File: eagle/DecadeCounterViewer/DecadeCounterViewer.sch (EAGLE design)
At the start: 16 parts, among them IC1 CD4017

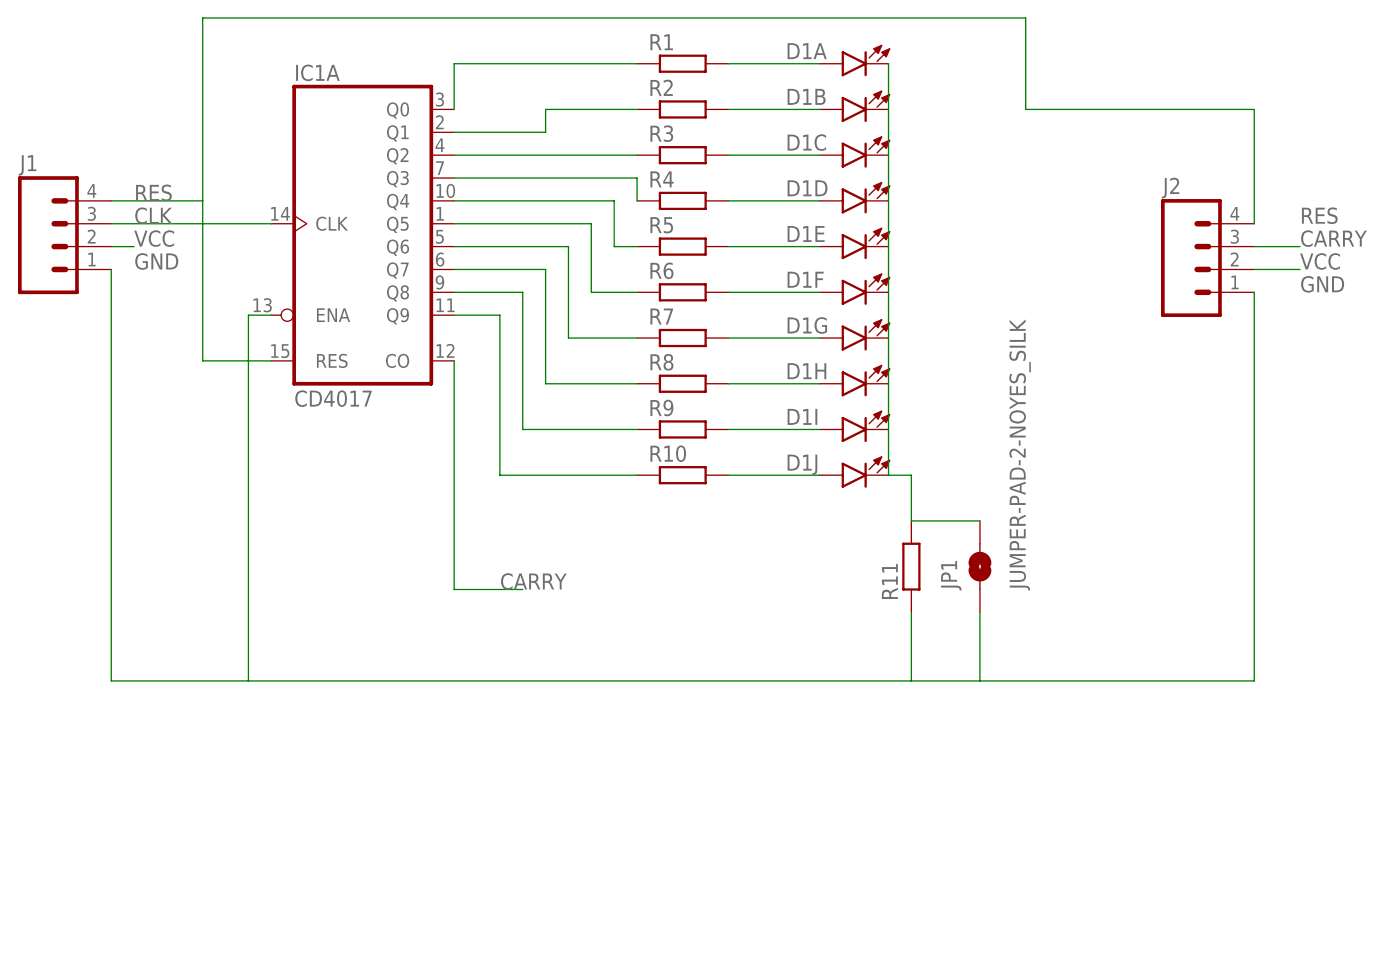
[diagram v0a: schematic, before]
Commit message: Decade counter continued
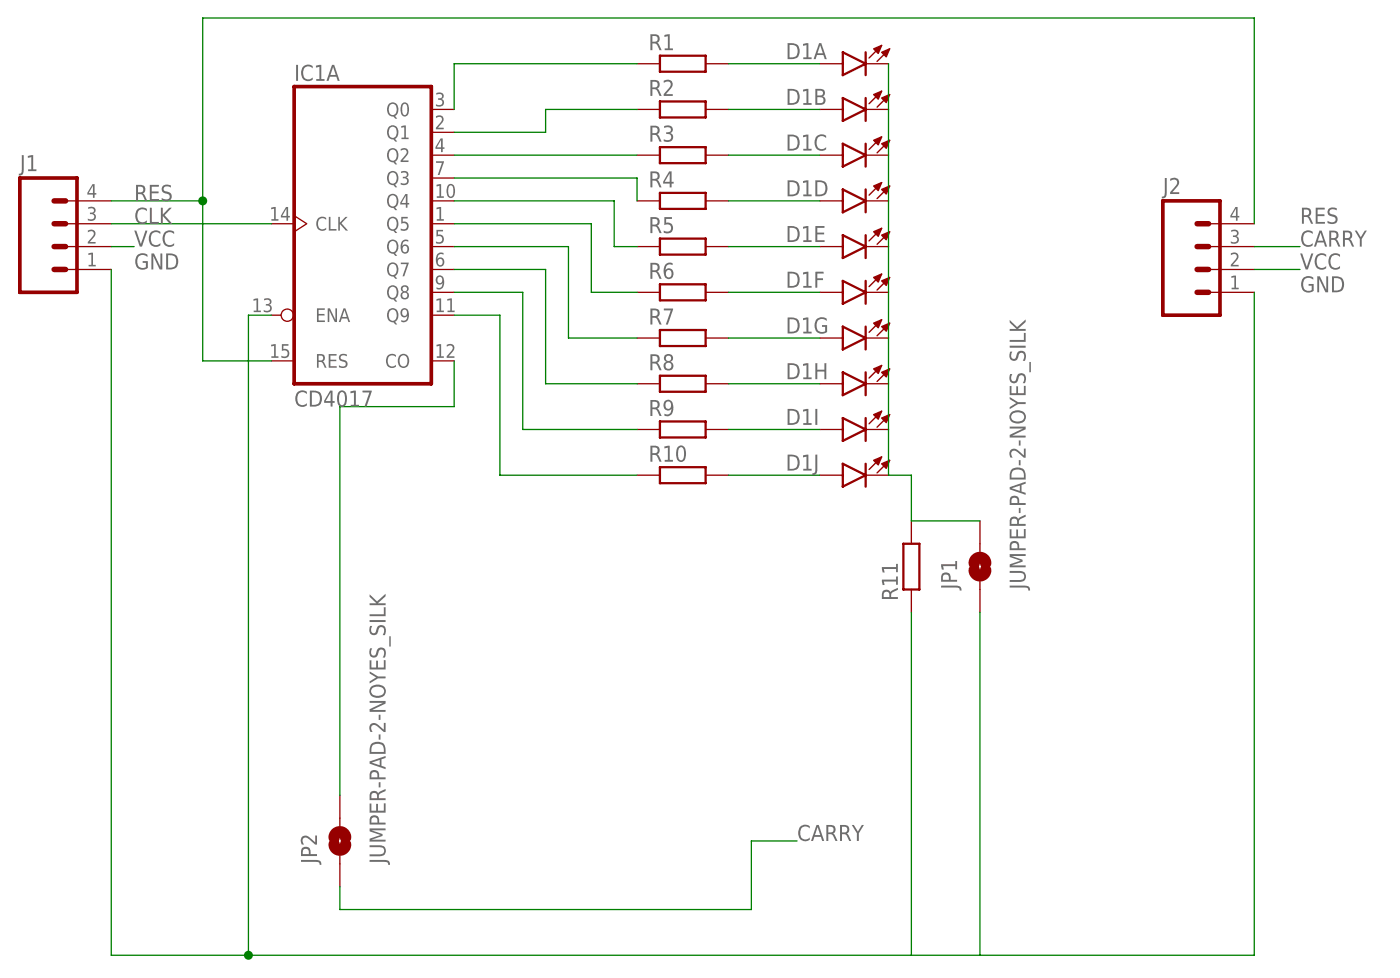
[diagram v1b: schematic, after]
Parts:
- added JP2: JUMPER-PAD-2-NOYES_SILK, SparkFun-Passives:JUMPER-PAD-2-NOYES_SILK
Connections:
- new net N$1: IC1A.CO, JP2.2
- net CARRY: now also JP2.1; no longer IC1A.CO
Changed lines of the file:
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@@
 <part name="J1" library="SparkFun-Connectors" deviceset="M04" device="LOCK"/>
 <part name="J2" library="SparkFun-Connectors" deviceset="M04" device="LOCK"/>
+<part name="JP2" library="SparkFun-Passives" deviceset="JUMPER-PAD-2-NO" device="YES_SILK"/>
 </parts>
 <sheets>
@@
 <instance part="J1" gate="G$1" x="-7.62" y="83.82"/>
 <instance part="J2" gate="G$1" x="119.38" y="81.28"/>
+<instance part="JP2" gate="G$1" x="22.86" y="17.78" rot="R90"/>
 </instances>
 <busses>
@@
 <segment>
 <pinref part="J1" gate="G$1" pin="1"/>
-<wire x1="-2.54" y1="81.28" x2="-2.54" y2="35.56" width="0.1524" layer="91"/>
+<wire x1="-2.54" y1="81.28" x2="-2.54" y2="5.08" width="0.1524" layer="91"/>
 <pinref part="R11" gate="G$1" pin="1"/>
-<wire x1="-2.54" y1="35.56" x2="12.7" y2="35.56" width="0.1524" layer="91"/>
-<wire x1="12.7" y1="35.56" x2="86.36" y2="35.56" width="0.1524" layer="91"/>
-<wire x1="86.36" y1="35.56" x2="86.36" y2="43.18" width="0.1524" layer="91"/>
+<wire x1="-2.54" y1="5.08" x2="12.7" y2="5.08" width="0.1524" layer="91"/>
+<wire x1="12.7" y1="5.08" x2="86.36" y2="5.08" width="0.1524" layer="91"/>
+<wire x1="86.36" y1="5.08" x2="86.36" y2="43.18" width="0.1524" layer="91"/>
 <pinref part="JP1" gate="G$1" pin="1"/>
-<wire x1="86.36" y1="35.56" x2="93.98" y2="35.56" width="0.1524" layer="91"/>
-<wire x1="93.98" y1="35.56" x2="93.98" y2="43.18" width="0.1524" layer="91"/>
+<wire x1="86.36" y1="5.08" x2="93.98" y2="5.08" width="0.1524" layer="91"/>
+<wire x1="93.98" y1="5.08" x2="93.98" y2="43.18" width="0.1524" layer="91"/>
 <label x="0" y="81.28" size="1.778" layer="95"/>
 <pinref part="IC1" gate="A" pin="ENA"/>
 <wire x1="15.24" y1="76.2" x2="12.7" y2="76.2" width="0.1524" layer="91"/>
-<wire x1="12.7" y1="76.2" x2="12.7" y2="35.56" width="0.1524" layer="91"/>
+<wire x1="12.7" y1="76.2" x2="12.7" y2="5.08" width="0.1524" layer="91"/>
 <pinref part="J2" gate="G$1" pin="1"/>
-<wire x1="93.98" y1="35.56" x2="124.46" y2="35.56" width="0.1524" layer="91"/>
-<wire x1="124.46" y1="35.56" x2="124.46" y2="78.74" width="0.1524" layer="91"/>
+<wire x1="93.98" y1="5.08" x2="124.46" y2="5.08" width="0.1524" layer="91"/>
+<wire x1="124.46" y1="5.08" x2="124.46" y2="78.74" width="0.1524" layer="91"/>
 <label x="129.54" y="78.74" size="1.778" layer="95"/>
+<junction x="12.7" y="5.08"/>
 </segment>
 </net>
@@
 <net name="CARRY" class="0">
 <segment>
-<pinref part="IC1" gate="A" pin="CO"/>
-<wire x1="35.56" y1="71.12" x2="35.56" y2="45.72" width="0.1524" layer="91"/>
-<wire x1="35.56" y1="45.72" x2="43.18" y2="45.72" width="0.1524" layer="91"/>
-<label x="40.64" y="45.72" size="1.778" layer="95"/>
+<wire x1="68.58" y1="17.78" x2="73.66" y2="17.78" width="0.1524" layer="91"/>
+<label x="73.66" y="17.78" size="1.778" layer="95"/>
+<pinref part="JP2" gate="G$1" pin="1"/>
+<wire x1="22.86" y1="12.7" x2="22.86" y2="10.16" width="0.1524" layer="91"/>
+<wire x1="22.86" y1="10.16" x2="68.58" y2="10.16" width="0.1524" layer="91"/>
+<wire x1="68.58" y1="10.16" x2="68.58" y2="17.78" width="0.1524" layer="91"/>
 </segment>
 <segment>
@@
 <label x="0" y="88.9" size="1.778" layer="95"/>
 <wire x1="7.62" y1="88.9" x2="7.62" y2="109.22" width="0.1524" layer="91"/>
-<wire x1="7.62" y1="109.22" x2="99.06" y2="109.22" width="0.1524" layer="91"/>
-<wire x1="99.06" y1="109.22" x2="99.06" y2="99.06" width="0.1524" layer="91"/>
+<wire x1="7.62" y1="109.22" x2="124.46" y2="109.22" width="0.1524" layer="91"/>
 <pinref part="J2" gate="G$1" pin="4"/>
-<wire x1="99.06" y1="99.06" x2="124.46" y2="99.06" width="0.1524" layer="91"/>
-<wire x1="124.46" y1="99.06" x2="124.46" y2="86.36" width="0.1524" layer="91"/>
+<wire x1="124.46" y1="109.22" x2="124.46" y2="86.36" width="0.1524" layer="91"/>
 <label x="129.54" y="86.36" size="1.778" layer="95"/>
-</segment>
-</net>
+<junction x="7.62" y="88.9"/>
+</segment>
+</net>
+<net name="N$1" class="0">
+<segment>
+<pinref part="IC1" gate="A" pin="CO"/>
+<wire x1="35.56" y1="71.12" x2="35.56" y2="66.04" width="0.1524" layer="91"/>
+<wire x1="35.56" y1="66.04" x2="22.86" y2="66.04" width="0.1524" layer="91"/>
+<pinref part="JP2" gate="G$1" pin="2"/>
+<wire x1="22.86" y1="66.04" x2="22.86" y2="22.86" width="0.1524" layer="91"/>
+</segment>
+</net>

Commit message: Added the decade counter board. Todo review and then send to production.
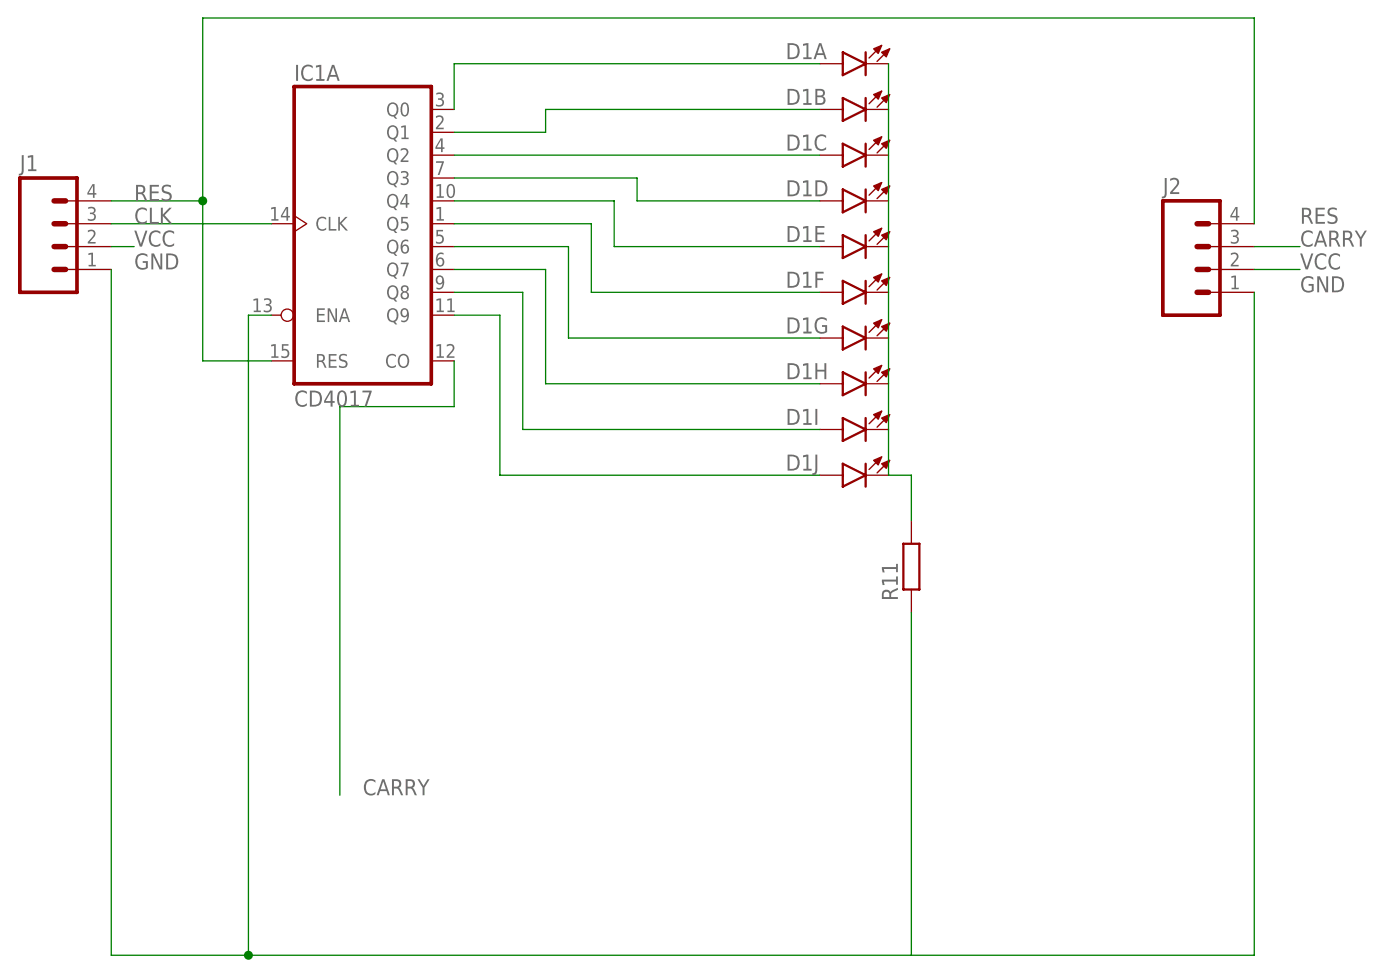
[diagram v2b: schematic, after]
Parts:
- removed JP1, JP2: JUMPER-PAD-2-NOYES_SILK, SparkFun-Passives:JUMPER-PAD-2-NOYES_SILK
- removed R1, R10, R2, R3, R4, R5, R6, R7, R8, R9: (no value), resistor:R-EU_R1206
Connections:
- removed net N$1: IC1A.CO, JP2.2
- removed net N$10: D1H.A, R8.2
- removed net N$11: D1I.A, R9.2
- removed net N$12: D1J.A, R10.2
- removed net N$3: D1A.A, R1.2
- removed net N$4: D1B.A, R2.2
- removed net N$5: D1C.A, R3.2
- removed net N$6: D1D.A, R4.2
- removed net N$7: D1E.A, R5.2
- removed net N$8: D1F.A, R6.2
- removed net N$9: D1G.A, R7.2
- net CARRY: now also IC1A.CO; no longer JP2.1
- net GND: no longer JP1.1
- net N$13: now also D1A.A; no longer R1.1
- net N$14: now also D1B.A; no longer R2.1
- net N$15: now also D1C.A; no longer R3.1
- net N$16: now also D1D.A; no longer R4.1
- net N$17: now also D1E.A; no longer R5.1
- net N$18: now also D1F.A; no longer R6.1
- net N$19: now also D1G.A; no longer R7.1
- net N$2: no longer JP1.2
- net N$20: now also D1H.A; no longer R8.1
- net N$21: now also D1I.A; no longer R9.1
- net N$22: now also D1J.A; no longer R10.1

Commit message: Added labels, reviewed. Ok for prod.
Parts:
- added R1: (no value), resistor:R-EU_0204/7
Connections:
- net GND: now also R1.1
- net N$2: now also R1.2
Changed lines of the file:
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@@
 <part name="J1" library="SparkFun-Connectors" deviceset="M04" device="LOCK"/>
 <part name="J2" library="SparkFun-Connectors" deviceset="M04" device="LOCK"/>
+<part name="R1" library="resistor" deviceset="R-EU_" device="0204/7"/>
 </parts>
 <sheets>
@@
 <instance part="J1" gate="G$1" x="-7.62" y="83.82"/>
 <instance part="J2" gate="G$1" x="119.38" y="81.28"/>
+<instance part="R1" gate="G$1" x="93.98" y="48.26" rot="R90"/>
 </instances>
 <busses>
@@
 <label x="129.54" y="78.74" size="1.778" layer="95"/>
 <junction x="12.7" y="5.08"/>
+<pinref part="R1" gate="G$1" pin="1"/>
+<wire x1="93.98" y1="43.18" x2="86.36" y2="43.18" width="0.1524" layer="91"/>
 </segment>
 </net>
@@
 <wire x1="83.82" y1="58.42" x2="86.36" y2="58.42" width="0.1524" layer="91"/>
 <wire x1="86.36" y1="58.42" x2="86.36" y2="53.34" width="0.1524" layer="91"/>
+<pinref part="R1" gate="G$1" pin="2"/>
+<wire x1="86.36" y1="53.34" x2="93.98" y2="53.34" width="0.1524" layer="91"/>
 </segment>
 </net>
